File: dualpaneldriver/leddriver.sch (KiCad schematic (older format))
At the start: 11 parts, among them J301 Conn_01x02, U301 LM3414HV

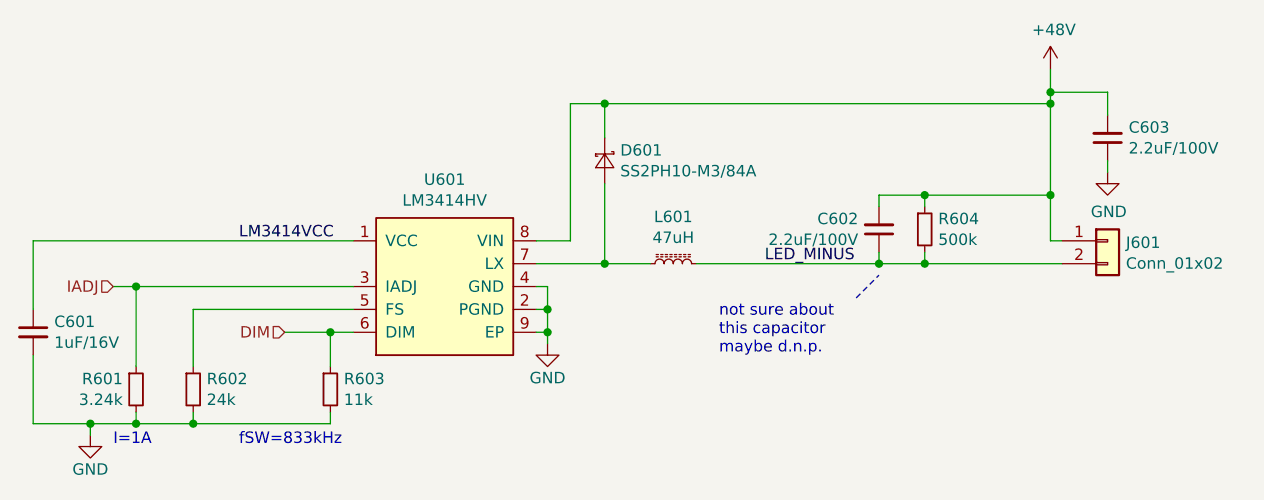
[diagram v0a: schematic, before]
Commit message: some components placed
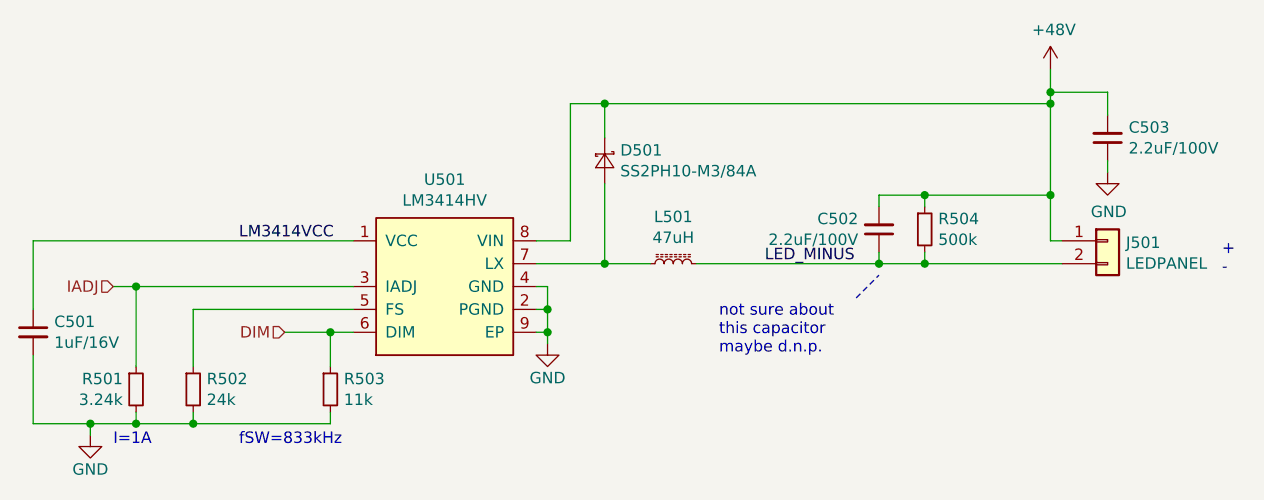
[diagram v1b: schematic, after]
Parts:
- C301: footprint (none) -> Capacitor_SMD:C_0603_1608Metric
- C302, C303: footprint (none) -> Capacitor_SMD:C_1206_3216Metric
- J301: value Conn_01x02 -> LEDPANEL
- R301, R302, R303, R304: footprint (none) -> Resistor_SMD:R_0603_1608Metric
- U301: footprint (none) -> Package_SO:SOIC-8-1EP_3.9x4.9mm_P1.27mm_EP2.29x3mm; V1 (none) -> LM3414HVMRX/NOPB
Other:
- note added: "+\n-"
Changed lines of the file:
@@
 $Descr A4 11693 8268
 encoding utf-8
-Sheet 3 6
+Sheet 5 6
 Title "Constant Current Buck LED Driver"
 Date "2019-11-25"
@@
 AR Path="/5DC91BAA/5DC2A6F0" Ref="L501"  Part="1"
 AR Path="/5DFBB68F/5DC2A6F0" Ref="L601"  Part="1"
-F 0 "L601" V 6755 3450 50  0000 C CNN
+F 0 "L501" V 6755 3450 50  0000 C CNN
 F 1 "47uH" V 6664 3450 50  0000 C CNN
 F 2 "Inductor_SMD:L_Bourns_SRN6045TA" H 6550 3450 50  0001 C CNN
@@
 AR Path="/5DC91BAA/5DC2D723" Ref="U501"  Part="1"
 AR Path="/5DFBB68F/5DC2D723" Ref="U601"  Part="1"
-F 0 "U601" H 5550 4018 50  0000 C CNN
+F 0 "U501" H 5550 4018 50  0000 C CNN
 F 1 "LM3414HV" H 5550 3927 50  0000 C CNN
-F 2 "" H 5450 3600 50  0001 C CNN
+F 2 "Package_SO:SOIC-8-1EP_3.9x4.9mm_P1.27mm_EP2.29x3mm" H 5450 3600 50  0001 C CNN
 F 3 "http://www.ti.com/lit/ds/symlink/lm3414hv.pdf" H 5450 3600 50  0001 C CNN
+F 4 "LM3414HVMRX/NOPB" H 5550 3550 50  0001 C CNN "V1"
 	1    5550 3550
 	1    0    0    -1
@@
 AR Path="/5DC91BAA/5DC3286F" Ref="C503"  Part="1"
 AR Path="/5DFBB68F/5DC3286F" Ref="C603"  Part="1"
-F 0 "C603" H 8358 2854 50  0000 R CNN
+F 0 "C503" H 8358 2854 50  0000 R CNN
 F 1 "2.2uF/100V" H 8358 2945 50  0000 R CNN
-F 2 "" H 8450 2900 50  0001 C CNN
+F 2 "Capacitor_SMD:C_1206_3216Metric" H 8450 2900 50  0001 C CNN
 F 3 "~" H 8450 2900 50  0001 C CNN
 	1    8450 2900
@@
 AR Path="/5DC91BAA/5DC338E9" Ref="J501"  Part="1"
 AR Path="/5DFBB68F/5DC338E9" Ref="J601"  Part="1"
-F 0 "J601" H 8530 3342 50  0000 L CNN
-F 1 "Conn_01x02" H 8530 3251 50  0000 L CNN
+F 0 "J501" H 8530 3342 50  0000 L CNN
+F 1 "LEDPANEL" H 8530 3251 50  0000 L CNN
 F 2 "Connector_PinHeader_2.54mm:PinHeader_1x02_P2.54mm_Vertical" H 8450 3350 50  0001 C CNN
 F 3 "~" H 8450 3350 50  0001 C CNN
@@
 AR Path="/5DC91BAA/5DC35DC1" Ref="D501"  Part="1"
 AR Path="/5DFBB68F/5DC35DC1" Ref="D601"  Part="1"
-F 0 "D601" V 6204 3068 50  0000 L CNN
+F 0 "D501" V 6204 3068 50  0000 L CNN
 F 1 "SS2PH10-M3/84A" V 6295 3068 50  0000 L CNN
 F 2 "Automated:D_SMP_DO-220AA" V 6250 3000 50  0001 C CNN
@@
 AR Path="/5DC91BAA/5DC49683" Ref="R502"  Part="1"
 AR Path="/5DFBB68F/5DC49683" Ref="R602"  Part="1"
-F 0 "R602" H 4509 4046 50  0000 L CNN
+F 0 "R502" H 4509 4046 50  0000 L CNN
 F 1 "24k" H 4509 3955 50  0000 L CNN
-F 2 "" H 4450 4000 50  0001 C CNN
+F 2 "Resistor_SMD:R_0603_1608Metric" H 4450 4000 50  0001 C CNN
 F 3 "~" H 4450 4000 50  0001 C CNN
 	1    4450 4000
@@
 AR Path="/5DC91BAA/5DC4BAC7" Ref="R501"  Part="1"
 AR Path="/5DFBB68F/5DC4BAC7" Ref="R601"  Part="1"
-F 0 "R601" H 4142 4046 50  0000 R CNN
+F 0 "R501" H 4142 4046 50  0000 R CNN
 F 1 "3.24k" H 4142 3955 50  0000 R CNN
-F 2 "" H 4200 4000 50  0001 C CNN
+F 2 "Resistor_SMD:R_0603_1608Metric" H 4200 4000 50  0001 C CNN
 F 3 "~" H 4200 4000 50  0001 C CNN
 	1    4200 4000
@@
 AR Path="/5DC91BAA/5DC50E25" Ref="C501"  Part="1"
 AR Path="/5DFBB68F/5DC50E25" Ref="C601"  Part="1"
-F 0 "C601" H 3842 3796 50  0000 L CNN
+F 0 "C501" H 3842 3796 50  0000 L CNN
 F 1 "1uF/16V" H 3842 3705 50  0000 L CNN
-F 2 "" H 3750 3750 50  0001 C CNN
+F 2 "Capacitor_SMD:C_0603_1608Metric" H 3750 3750 50  0001 C CNN
 F 3 "~" H 3750 3750 50  0001 C CNN
 	1    3750 3750
@@
 AR Path="/5DC91BAA/5DC67FF2" Ref="C502"  Part="1"
 AR Path="/5DFBB68F/5DC67FF2" Ref="C602"  Part="1"
-F 0 "C602" H 7541 3254 50  0000 L CNN
+F 0 "C502" H 7541 3254 50  0000 L CNN
 F 1 "2.2uF/100V" H 7541 3345 50  0000 L CNN
-F 2 "" H 7450 3300 50  0001 C CNN
+F 2 "Capacitor_SMD:C_1206_3216Metric" H 7450 3300 50  0001 C CNN
 F 3 "~" H 7450 3300 50  0001 C CNN
 	1    7450 3300
@@
 AR Path="/5DC91BAA/5DC7A9E7" Ref="R504"  Part="1"
 AR Path="/5DFBB68F/5DC7A9E7" Ref="R604"  Part="1"
-F 0 "R604" H 7709 3346 50  0000 L CNN
+F 0 "R504" H 7709 3346 50  0000 L CNN
 F 1 "500k" H 7709 3255 50  0000 L CNN
-F 2 "" H 7650 3300 50  0001 C CNN
+F 2 "Resistor_SMD:R_0603_1608Metric" H 7650 3300 50  0001 C CNN
 F 3 "~" H 7650 3300 50  0001 C CNN
 	1    7650 3300
@@
 AR Path="/5DC91BAA/5DC82C0A" Ref="R503"  Part="1"
 AR Path="/5DFBB68F/5DC82C0A" Ref="R603"  Part="1"
-F 0 "R603" H 5109 4046 50  0000 L CNN
+F 0 "R503" H 5109 4046 50  0000 L CNN
 F 1 "11k" H 5109 3955 50  0000 L CNN
-F 2 "" H 5050 4000 50  0001 C CNN
+F 2 "Resistor_SMD:R_0603_1608Metric" H 5050 4000 50  0001 C CNN
 F 3 "~" H 5050 4000 50  0001 C CNN
 	1    5050 4000
@@
 Wire Notes Line
 	7350 3600 7450 3500
+Text Notes 8950 3500 0    50   ~ 0
++\n-
 $EndSCHEMATC

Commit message: i'm too sleepy to continue
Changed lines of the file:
@@
 AR Path="/5DC91BAA/5DC2A6F0" Ref="L501"  Part="1"
 AR Path="/5DFBB68F/5DC2A6F0" Ref="L601"  Part="1"
-F 0 "L501" V 6755 3450 50  0000 C CNN
+F 0 "L601" V 6755 3450 50  0000 C CNN
 F 1 "47uH" V 6664 3450 50  0000 C CNN
 F 2 "Inductor_SMD:L_Bourns_SRN6045TA" H 6550 3450 50  0001 C CNN
@@
 AR Path="/5DC91BAA/5DC2D723" Ref="U501"  Part="1"
 AR Path="/5DFBB68F/5DC2D723" Ref="U601"  Part="1"
-F 0 "U501" H 5550 4018 50  0000 C CNN
+F 0 "U601" H 5550 4018 50  0000 C CNN
 F 1 "LM3414HV" H 5550 3927 50  0000 C CNN
 F 2 "Package_SO:SOIC-8-1EP_3.9x4.9mm_P1.27mm_EP2.29x3mm" H 5450 3600 50  0001 C CNN
@@
 AR Path="/5DC91BAA/5DC3286F" Ref="C503"  Part="1"
 AR Path="/5DFBB68F/5DC3286F" Ref="C603"  Part="1"
-F 0 "C503" H 8358 2854 50  0000 R CNN
+F 0 "C603" H 8358 2854 50  0000 R CNN
 F 1 "2.2uF/100V" H 8358 2945 50  0000 R CNN
 F 2 "Capacitor_SMD:C_1206_3216Metric" H 8450 2900 50  0001 C CNN
@@
 AR Path="/5DC91BAA/5DC338E9" Ref="J501"  Part="1"
 AR Path="/5DFBB68F/5DC338E9" Ref="J601"  Part="1"
-F 0 "J501" H 8530 3342 50  0000 L CNN
+F 0 "J601" H 8530 3342 50  0000 L CNN
 F 1 "LEDPANEL" H 8530 3251 50  0000 L CNN
 F 2 "Connector_PinHeader_2.54mm:PinHeader_1x02_P2.54mm_Vertical" H 8450 3350 50  0001 C CNN
@@
 AR Path="/5DC91BAA/5DC35DC1" Ref="D501"  Part="1"
 AR Path="/5DFBB68F/5DC35DC1" Ref="D601"  Part="1"
-F 0 "D501" V 6204 3068 50  0000 L CNN
+F 0 "D601" V 6204 3068 50  0000 L CNN
 F 1 "SS2PH10-M3/84A" V 6295 3068 50  0000 L CNN
 F 2 "Automated:D_SMP_DO-220AA" V 6250 3000 50  0001 C CNN
@@
 AR Path="/5DC91BAA/5DC49683" Ref="R502"  Part="1"
 AR Path="/5DFBB68F/5DC49683" Ref="R602"  Part="1"
-F 0 "R502" H 4509 4046 50  0000 L CNN
+F 0 "R602" H 4509 4046 50  0000 L CNN
 F 1 "24k" H 4509 3955 50  0000 L CNN
 F 2 "Resistor_SMD:R_0603_1608Metric" H 4450 4000 50  0001 C CNN
@@
 AR Path="/5DC91BAA/5DC4BAC7" Ref="R501"  Part="1"
 AR Path="/5DFBB68F/5DC4BAC7" Ref="R601"  Part="1"
-F 0 "R501" H 4142 4046 50  0000 R CNN
+F 0 "R601" H 4142 4046 50  0000 R CNN
 F 1 "3.24k" H 4142 3955 50  0000 R CNN
 F 2 "Resistor_SMD:R_0603_1608Metric" H 4200 4000 50  0001 C CNN
@@
 AR Path="/5DC91BAA/5DC50E25" Ref="C501"  Part="1"
 AR Path="/5DFBB68F/5DC50E25" Ref="C601"  Part="1"
-F 0 "C501" H 3842 3796 50  0000 L CNN
+F 0 "C601" H 3842 3796 50  0000 L CNN
 F 1 "1uF/16V" H 3842 3705 50  0000 L CNN
 F 2 "Capacitor_SMD:C_0603_1608Metric" H 3750 3750 50  0001 C CNN
@@
 AR Path="/5DC91BAA/5DC67FF2" Ref="C502"  Part="1"
 AR Path="/5DFBB68F/5DC67FF2" Ref="C602"  Part="1"
-F 0 "C502" H 7541 3254 50  0000 L CNN
+F 0 "C602" H 7541 3254 50  0000 L CNN
 F 1 "2.2uF/100V" H 7541 3345 50  0000 L CNN
 F 2 "Capacitor_SMD:C_1206_3216Metric" H 7450 3300 50  0001 C CNN
@@
 AR Path="/5DC91BAA/5DC7A9E7" Ref="R504"  Part="1"
 AR Path="/5DFBB68F/5DC7A9E7" Ref="R604"  Part="1"
-F 0 "R504" H 7709 3346 50  0000 L CNN
+F 0 "R604" H 7709 3346 50  0000 L CNN
 F 1 "500k" H 7709 3255 50  0000 L CNN
 F 2 "Resistor_SMD:R_0603_1608Metric" H 7650 3300 50  0001 C CNN
@@
 AR Path="/5DC91BAA/5DC82C0A" Ref="R503"  Part="1"
 AR Path="/5DFBB68F/5DC82C0A" Ref="R603"  Part="1"
-F 0 "R503" H 5109 4046 50  0000 L CNN
+F 0 "R603" H 5109 4046 50  0000 L CNN
 F 1 "11k" H 5109 3955 50  0000 L CNN
 F 2 "Resistor_SMD:R_0603_1608Metric" H 5050 4000 50  0001 C CNN

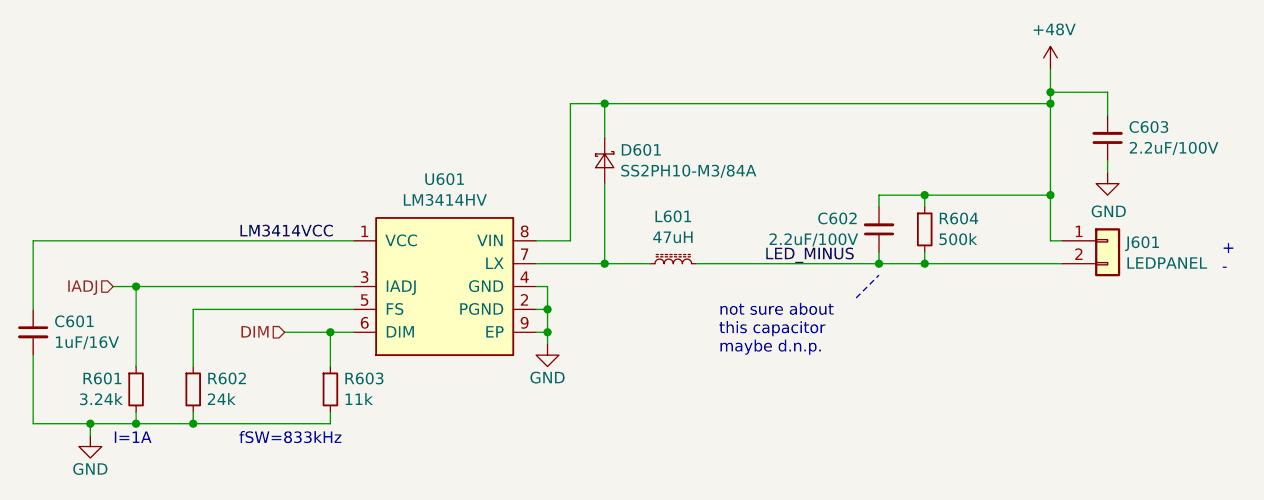
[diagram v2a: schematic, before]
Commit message: 100% routed, silkscreen still fucked up
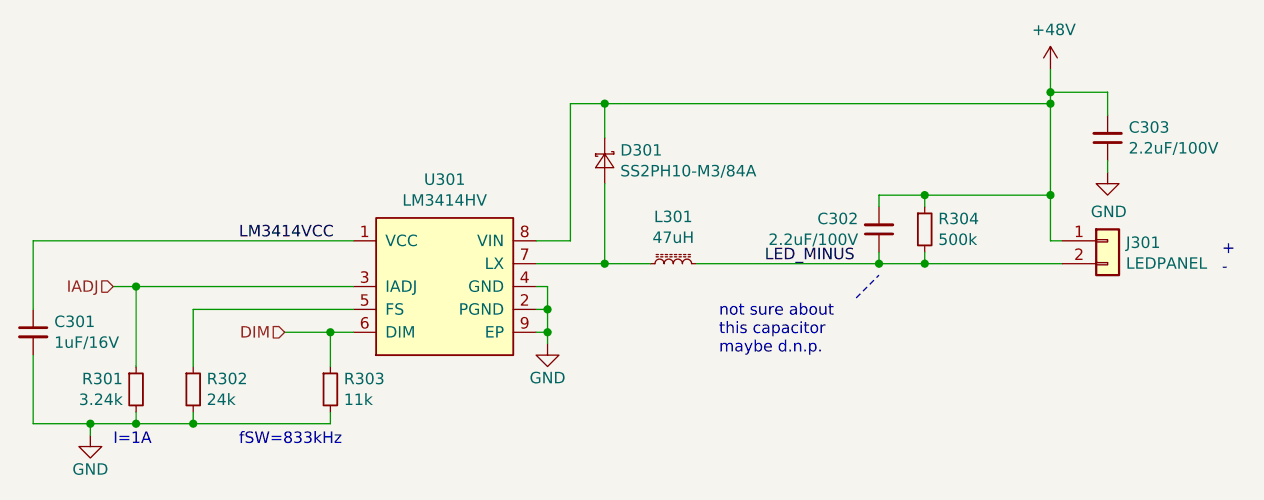
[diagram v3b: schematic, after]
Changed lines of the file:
@@
 $Descr A4 11693 8268
 encoding utf-8
-Sheet 5 6
+Sheet 3 6
 Title "Constant Current Buck LED Driver"
 Date "2019-11-25"
@@
 AR Path="/5DC91BAA/5DC2A6F0" Ref="L501"  Part="1"
 AR Path="/5DFBB68F/5DC2A6F0" Ref="L601"  Part="1"
-F 0 "L601" V 6755 3450 50  0000 C CNN
+F 0 "L301" V 6755 3450 50  0000 C CNN
 F 1 "47uH" V 6664 3450 50  0000 C CNN
 F 2 "Inductor_SMD:L_Bourns_SRN6045TA" H 6550 3450 50  0001 C CNN
@@
 AR Path="/5DC91BAA/5DC2D723" Ref="U501"  Part="1"
 AR Path="/5DFBB68F/5DC2D723" Ref="U601"  Part="1"
-F 0 "U601" H 5550 4018 50  0000 C CNN
+F 0 "U301" H 5550 4018 50  0000 C CNN
 F 1 "LM3414HV" H 5550 3927 50  0000 C CNN
 F 2 "Package_SO:SOIC-8-1EP_3.9x4.9mm_P1.27mm_EP2.29x3mm" H 5450 3600 50  0001 C CNN
@@
 AR Path="/5DC91BAA/5DC3286F" Ref="C503"  Part="1"
 AR Path="/5DFBB68F/5DC3286F" Ref="C603"  Part="1"
-F 0 "C603" H 8358 2854 50  0000 R CNN
+F 0 "C303" H 8358 2854 50  0000 R CNN
 F 1 "2.2uF/100V" H 8358 2945 50  0000 R CNN
 F 2 "Capacitor_SMD:C_1206_3216Metric" H 8450 2900 50  0001 C CNN
@@
 AR Path="/5DC91BAA/5DC32F9A" Ref="#PWR0503"  Part="1"
 AR Path="/5DFBB68F/5DC32F9A" Ref="#PWR0603"  Part="1"
-F 0 "#PWR0603" H 8200 2450 50  0001 C CNN
+F 0 "#PWR0303" H 8200 2450 50  0001 C CNN
 F 1 "+48V" H 8215 2773 50  0000 C CNN
 F 2 "" H 8200 2600 50  0001 C CNN
@@
 AR Path="/5DC91BAA/5DC338E9" Ref="J501"  Part="1"
 AR Path="/5DFBB68F/5DC338E9" Ref="J601"  Part="1"
-F 0 "J601" H 8530 3342 50  0000 L CNN
+F 0 "J301" H 8530 3342 50  0000 L CNN
 F 1 "LEDPANEL" H 8530 3251 50  0000 L CNN
 F 2 "Connector_PinHeader_2.54mm:PinHeader_1x02_P2.54mm_Vertical" H 8450 3350 50  0001 C CNN
@@
 AR Path="/5DC91BAA/5DC35DC1" Ref="D501"  Part="1"
 AR Path="/5DFBB68F/5DC35DC1" Ref="D601"  Part="1"
-F 0 "D601" V 6204 3068 50  0000 L CNN
+F 0 "D301" V 6204 3068 50  0000 L CNN
 F 1 "SS2PH10-M3/84A" V 6295 3068 50  0000 L CNN
 F 2 "Automated:D_SMP_DO-220AA" V 6250 3000 50  0001 C CNN
@@
 AR Path="/5DC91BAA/5DC38935" Ref="#PWR0504"  Part="1"
 AR Path="/5DFBB68F/5DC38935" Ref="#PWR0604"  Part="1"
-F 0 "#PWR0604" H 8450 2800 50  0001 C CNN
+F 0 "#PWR0304" H 8450 2800 50  0001 C CNN
 F 1 "GND" H 8455 2877 50  0000 C CNN
 F 2 "" H 8450 3050 50  0001 C CNN
@@
 AR Path="/5DC91BAA/5DC438A5" Ref="#PWR0502"  Part="1"
 AR Path="/5DFBB68F/5DC438A5" Ref="#PWR0602"  Part="1"
-F 0 "#PWR0602" H 6000 3550 50  0001 C CNN
+F 0 "#PWR0302" H 6000 3550 50  0001 C CNN
 F 1 "GND" H 6000 3650 50  0000 C CNN
 F 2 "" H 6000 3800 50  0001 C CNN
@@
 AR Path="/5DC91BAA/5DC49683" Ref="R502"  Part="1"
 AR Path="/5DFBB68F/5DC49683" Ref="R602"  Part="1"
-F 0 "R602" H 4509 4046 50  0000 L CNN
+F 0 "R302" H 4509 4046 50  0000 L CNN
 F 1 "24k" H 4509 3955 50  0000 L CNN
 F 2 "Resistor_SMD:R_0603_1608Metric" H 4450 4000 50  0001 C CNN
@@
 AR Path="/5DC91BAA/5DC4BAC7" Ref="R501"  Part="1"
 AR Path="/5DFBB68F/5DC4BAC7" Ref="R601"  Part="1"
-F 0 "R601" H 4142 4046 50  0000 R CNN
+F 0 "R301" H 4142 4046 50  0000 R CNN
 F 1 "3.24k" H 4142 3955 50  0000 R CNN
 F 2 "Resistor_SMD:R_0603_1608Metric" H 4200 4000 50  0001 C CNN
@@
 AR Path="/5DC91BAA/5DC50E25" Ref="C501"  Part="1"
 AR Path="/5DFBB68F/5DC50E25" Ref="C601"  Part="1"
-F 0 "C601" H 3842 3796 50  0000 L CNN
+F 0 "C301" H 3842 3796 50  0000 L CNN
 F 1 "1uF/16V" H 3842 3705 50  0000 L CNN
 F 2 "Capacitor_SMD:C_0603_1608Metric" H 3750 3750 50  0001 C CNN
@@
 AR Path="/5DC91BAA/5DC51B06" Ref="#PWR0501"  Part="1"
 AR Path="/5DFBB68F/5DC51B06" Ref="#PWR0601"  Part="1"
-F 0 "#PWR0601" H 4000 3950 50  0001 C CNN
+F 0 "#PWR0301" H 4000 3950 50  0001 C CNN
 F 1 "GND" H 4000 4050 50  0000 C CNN
 F 2 "" H 4000 4200 50  0001 C CNN
@@
 AR Path="/5DC91BAA/5DC67FF2" Ref="C502"  Part="1"
 AR Path="/5DFBB68F/5DC67FF2" Ref="C602"  Part="1"
-F 0 "C602" H 7541 3254 50  0000 L CNN
+F 0 "C302" H 7541 3254 50  0000 L CNN
 F 1 "2.2uF/100V" H 7541 3345 50  0000 L CNN
 F 2 "Capacitor_SMD:C_1206_3216Metric" H 7450 3300 50  0001 C CNN
@@
 AR Path="/5DC91BAA/5DC7A9E7" Ref="R504"  Part="1"
 AR Path="/5DFBB68F/5DC7A9E7" Ref="R604"  Part="1"
-F 0 "R604" H 7709 3346 50  0000 L CNN
+F 0 "R304" H 7709 3346 50  0000 L CNN
 F 1 "500k" H 7709 3255 50  0000 L CNN
 F 2 "Resistor_SMD:R_0603_1608Metric" H 7650 3300 50  0001 C CNN
@@
 AR Path="/5DC91BAA/5DC82C0A" Ref="R503"  Part="1"
 AR Path="/5DFBB68F/5DC82C0A" Ref="R603"  Part="1"
-F 0 "R603" H 5109 4046 50  0000 L CNN
+F 0 "R303" H 5109 4046 50  0000 L CNN
 F 1 "11k" H 5109 3955 50  0000 L CNN
 F 2 "Resistor_SMD:R_0603_1608Metric" H 5050 4000 50  0001 C CNN
